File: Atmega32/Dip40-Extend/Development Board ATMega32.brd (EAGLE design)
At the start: 86.4 x 57.1 mm, 63 parts, among them IC1 REG1117, IC2 MEGA32-P, IC3 7805T, P1 PIN-BIG1X, P10 PIN-BIG1X, P11 PIN-BIG1X, P12 PIN-BIG1X, P13 PIN-BIG1X, P14 PIN-BIG1X, P15 PIN-BIG1X, P16 PIN-BIG1X, P17 PIN-BIG1X, P18 PIN-BIG1X, P19 PIN-BIG1X, P2 PIN-BIG1X, P20 PIN-BIG1X, P21 PIN-BIG1X, P22 PIN-BIG1X, P23 PIN-BIG1X, P24 PIN-BIG1X, P25 PIN-BIG1X, P26 PIN-BIG1X, P3 PIN-BIG1X, P4 PIN-BIG1X, P5 PIN-BIG1X, P6 PIN-BIG1X, P7 PIN-BIG1X, P8 PIN-BIG1X, P9 PIN-BIG1X, Q3 16m, SW2 smd_sw, X1 PN61729-S, X3 057-010-1

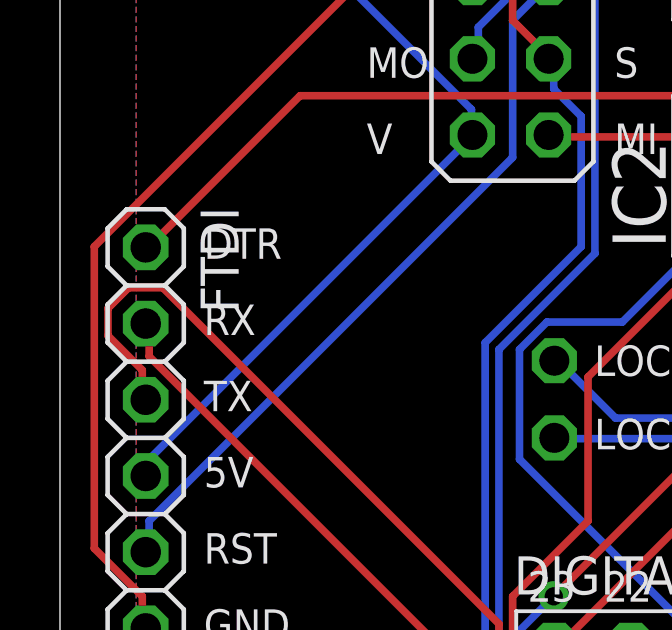
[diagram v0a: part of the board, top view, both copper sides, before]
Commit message: update Atemga32 Extends Dip40
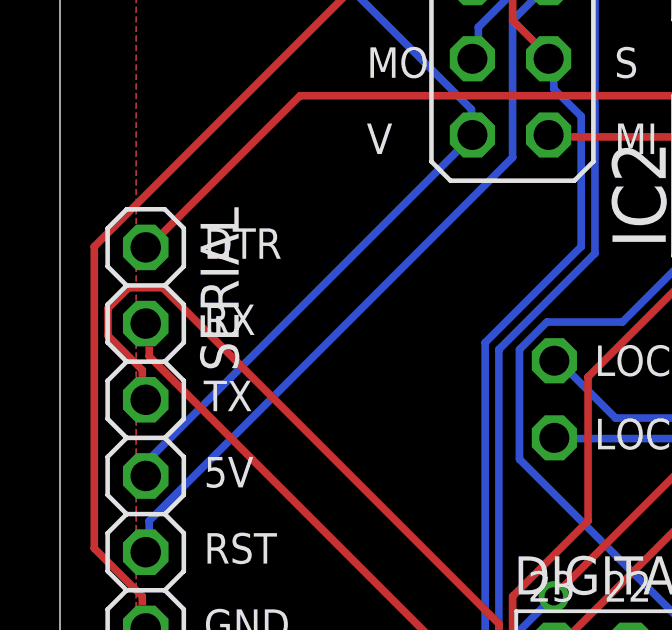
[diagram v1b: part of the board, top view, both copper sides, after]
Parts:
- renumbered FTDI to SERIAL
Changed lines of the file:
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@@
 <element name="P16" library="ioshub" package="PIN-BIG" value="PIN-BIG1X" x="6.985" y="43.815"/>
 <element name="P17" library="ioshub" package="PIN-BIG" value="PIN-BIG1X" x="1.905" y="43.815"/>
-<element name="FTDI" library="adafruit" package="1X06" value="6H" x="2.8575" y="13.97" rot="R270"/>
+<element name="SERIAL" library="adafruit" package="1X06" value="6H" x="2.8575" y="13.97" rot="R270"/>
 <element name="P9" library="ioshub" package="PIN-BIG" value="PIN-BIG1X" x="9.525" y="40.3225"/>
 <element name="P18" library="ioshub" package="PIN-BIG" value="PIN-BIG1X" x="4.445" y="40.3225"/>
@@
 <contactref element="LED_ASP" pad="C"/>
 <contactref element="P17" pad="P$1"/>
-<contactref element="FTDI" pad="6"/>
+<contactref element="SERIAL" pad="6"/>
 <contactref element="P20" pad="P$1"/>
 <contactref element="P24" pad="P$1"/>
@@
 <contactref element="R1" pad="1"/>
 <contactref element="P14" pad="P$1"/>
-<contactref element="FTDI" pad="4"/>
+<contactref element="SERIAL" pad="4"/>
 <contactref element="P9" pad="P$1"/>
 <contactref element="P21" pad="P$1"/>
@@
 <contactref element="VOLT_HEADER" pad="6"/>
 <contactref element="P4" pad="P$1"/>
-<contactref element="FTDI" pad="5"/>
+<contactref element="SERIAL" pad="5"/>
 <wire x1="64.9224" y1="13.0302" x2="64.9224" y2="14.4018" width="0.254" layer="1"/>
 <wire x1="65.151" y1="12.8016" x2="64.9224" y2="13.0302" width="0.254" layer="1"/>
@@
 <contactref element="IC2" pad="14"/>
 <contactref element="DIGITAL8_HEADER" pad="8"/>
-<contactref element="FTDI" pad="2"/>
+<contactref element="SERIAL" pad="2"/>
 <wire x1="55.5498" y1="18.5166" x2="55.5498" y2="18.9738" width="0.254" layer="1"/>
 <wire x1="53.2638" y1="16.2306" x2="55.5498" y2="18.5166" width="0.254" layer="1"/>
@@
 <contactref element="DIGITAL8_HEADER" pad="7"/>
 <contactref element="IC2" pad="15"/>
-<contactref element="FTDI" pad="3"/>
+<contactref element="SERIAL" pad="3"/>
 <wire x1="58.293" y1="15.0876" x2="58.293" y2="19.01825" width="0.254" layer="1"/>
 <wire x1="54.4068" y1="11.2014" x2="58.293" y2="15.0876" width="0.254" layer="1"/>
@@
 <signal name="DTR">
 <contactref element="C12" pad="1"/>
-<contactref element="FTDI" pad="1"/>
+<contactref element="SERIAL" pad="1"/>
 <wire x1="8.001" y1="25.3746" x2="34.0614" y2="25.3746" width="0.254" layer="1"/>
 <wire x1="2.9718" y1="20.3454" x2="8.001" y2="25.3746" width="0.254" layer="1"/>
